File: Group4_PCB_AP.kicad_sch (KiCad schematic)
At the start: 89 parts, among them J18 Conn_Coaxial, J19 Conn_Coaxial, J20 Conn_02x02_Odd_Even, J21 Conn_02x02_Odd_Even, J22 Conn_Coaxial, J23 Conn_Coaxial, J24 Conn_02x02_Odd_Even, J25 Conn_02x02_Odd_Even, J26 Conn_02x02_Odd_Even, J27 Conn_02x02_Odd_Even, J28 Conn_02x02_Odd_Even, J29 Conn_Coaxial, J30 Conn_Coaxial, J31 Conn_02x02_Odd_Even, J32 Conn_02x02_Odd_Even, J33 Conn_02x02_Odd_Even

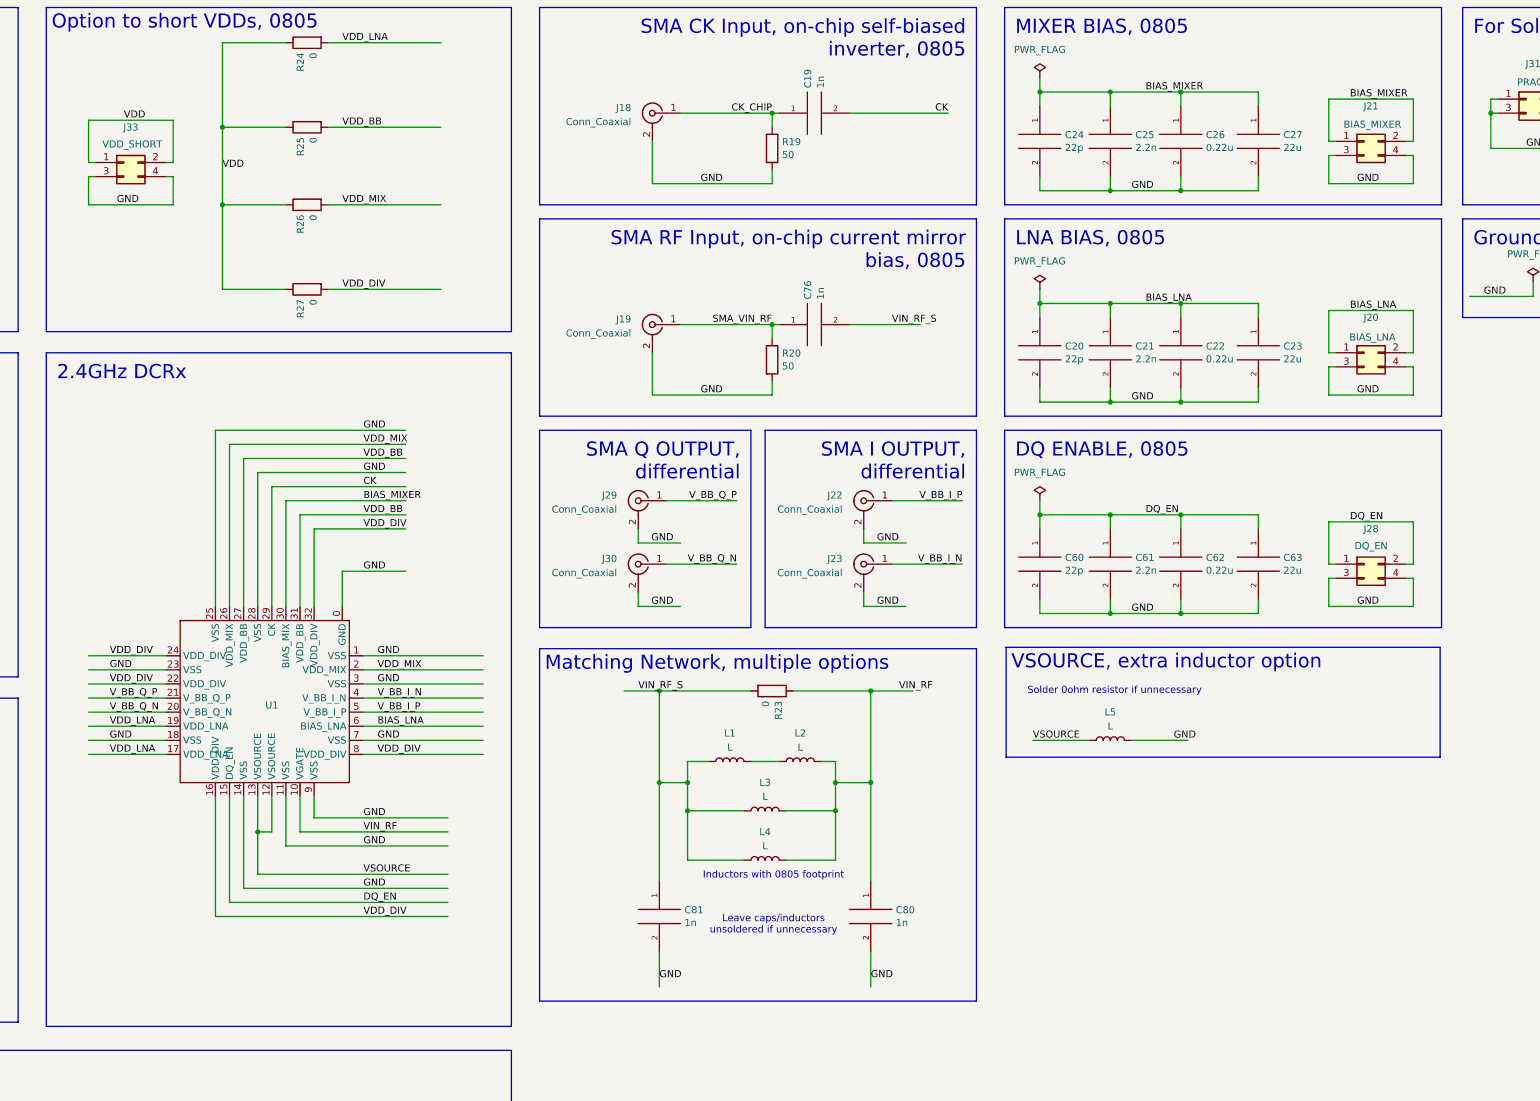
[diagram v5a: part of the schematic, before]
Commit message: Cleaned up matching network
Cleaned up schematic and layout for matching network, removed termination and 0 ohm resistors, removed probe points on all RF traces. Removed zero ohm from VSOURCE
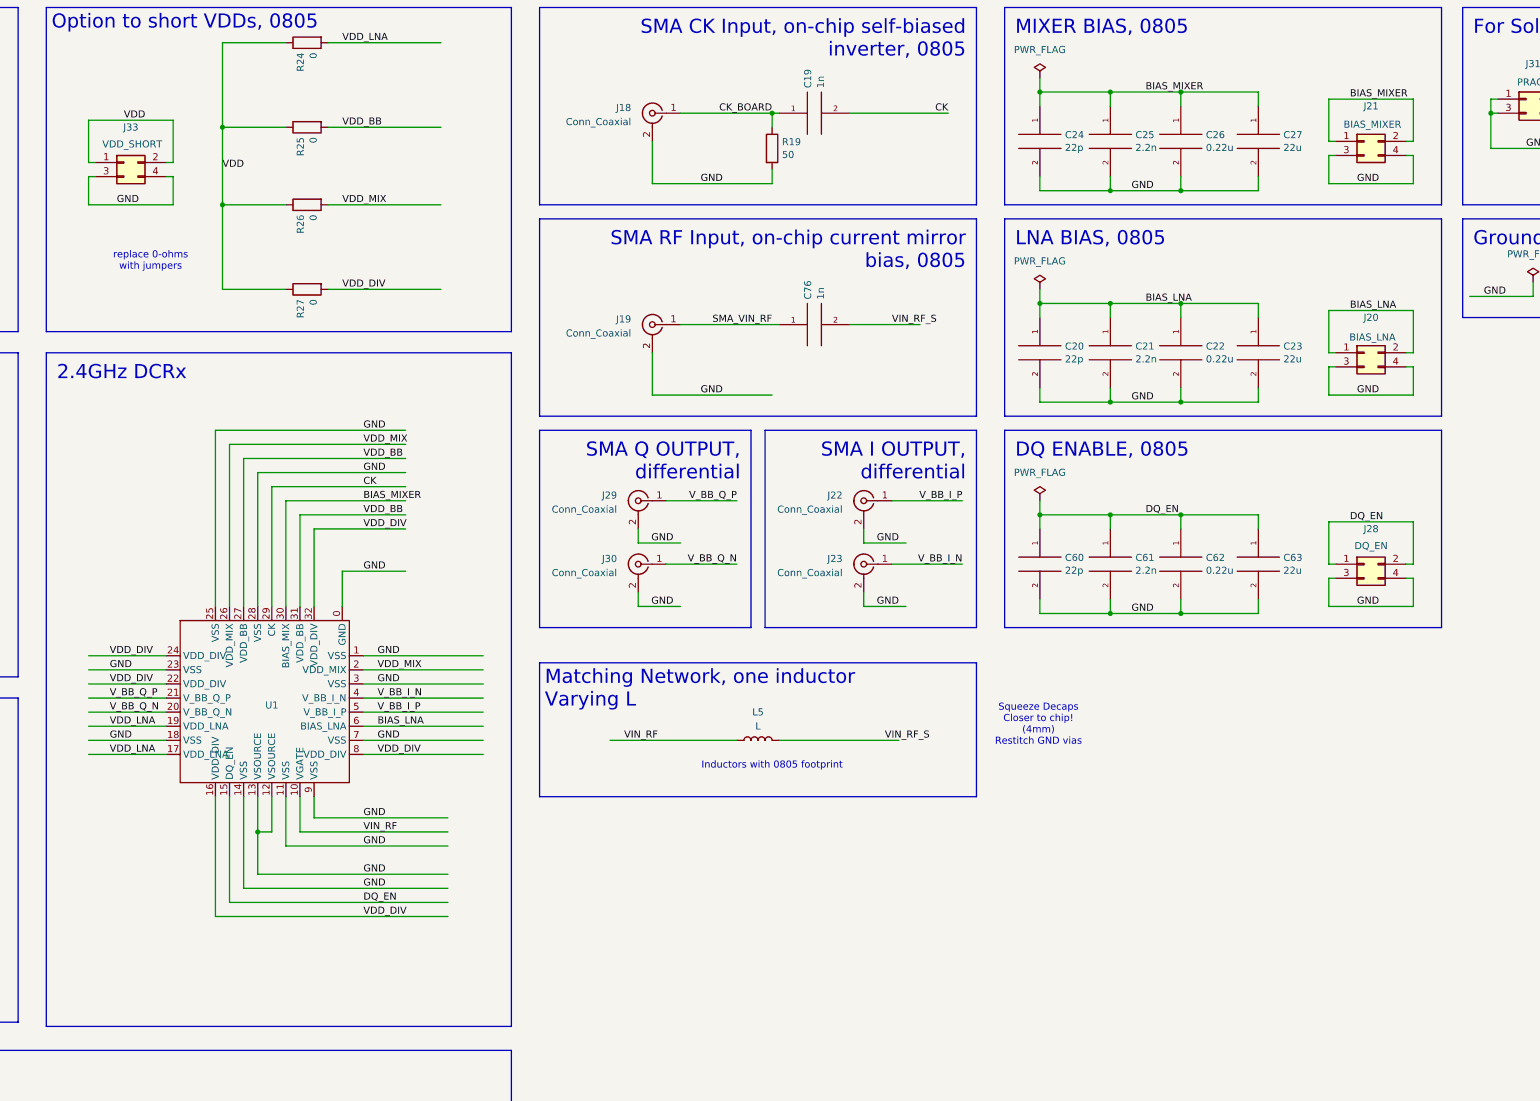
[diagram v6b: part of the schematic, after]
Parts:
- removed C80, C81: 1n, Capacitor_SMD:C_0805_2012Metric_Pad1.18x1.45mm_HandSolder, symbol pspice:C
- removed L1, L2, L3, L4: L, Inductor_SMD:L_0805_2012Metric_Pad1.15x1.40mm_HandSolder, symbol Device:L
- removed R20: 50, Resistor_SMD:R_0805_2012Metric_Pad1.20x1.40mm_HandSolder, symbol Device:R
- removed R23: 0, Resistor_SMD:R_0805_2012Metric_Pad1.20x1.40mm_HandSolder, symbol Device:R
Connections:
- net GND: now also U1.12 (VSOURCE), U1.13 (VSOURCE); no longer L5.1
- net VIN_RF: now also L5.2
- net VIN_RF_S: now also L5.1
- net CK_CHIP renamed CK_BOARD
- removed net VSOURCE: L5.2, U1.12 (VSOURCE), U1.13 (VSOURCE)
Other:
- note added: "Squeeze Decaps Closer to chip! (4mm) Restitch GND vias"
- note added: "replace 0-ohms with jumpers"
- note removed: "Leave caps/inductors unsoldered if unnecessary"
- note removed: "Solder 0ohm resistor if unnecessary"

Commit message: Added UCLA Silk Screen and Gerber files
Finalized PCB and made Gerber files
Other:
- note removed: "Squeeze Decaps Closer to chip! (4mm) Restitch GND vias"
- note removed: "replace 0-ohms with jumpers"
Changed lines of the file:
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@@
 	(generator_version "9.0")
 	(paper "A3")
-	(text "replace 0-ohms\nwith jumpers"
-		(exclude_from_sim no)
-		(at 119.126 60.96 0)
-		(effects
-			(font
-				(size 1.27 1.27)
-			)
-		)
-	)
 	(text "Inductors with 0805 footprint\n"
 		(exclude_from_sim no)
@@
 		(effects
 			(font
-				(size 1.27 1.27)
-			)
-		)
-	)
-	(text "Squeeze Decaps\nCloser to chip! \n(4mm)\nRestitch GND vias"
-		(exclude_from_sim no)
-		(at 279.146 144.526 0)
-		(effects
-			(font
